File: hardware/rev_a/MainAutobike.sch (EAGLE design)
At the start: 137 parts, among them J13 TC2030-CTX, U1 ATUM, U2 PCA9685, U3 PCA9685, U4 ADXL362

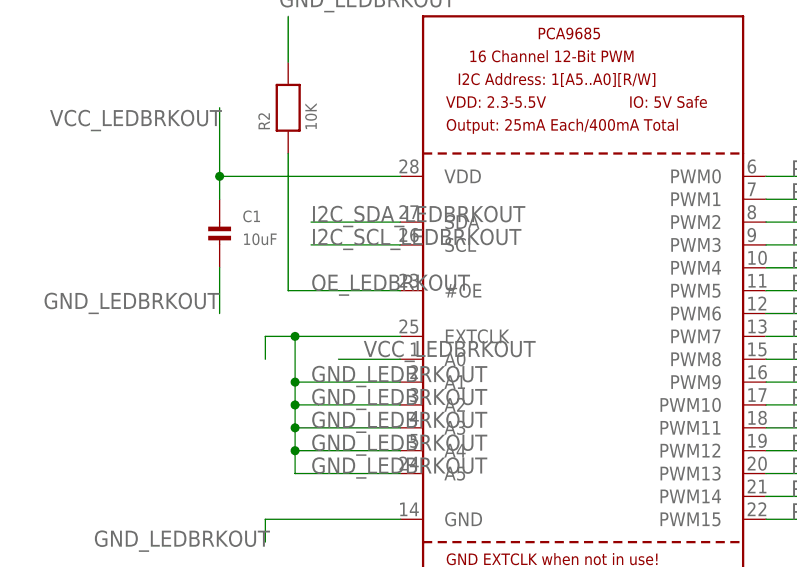
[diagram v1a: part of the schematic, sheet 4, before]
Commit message: charles, look over hall effect please; checked rest of schematic and board
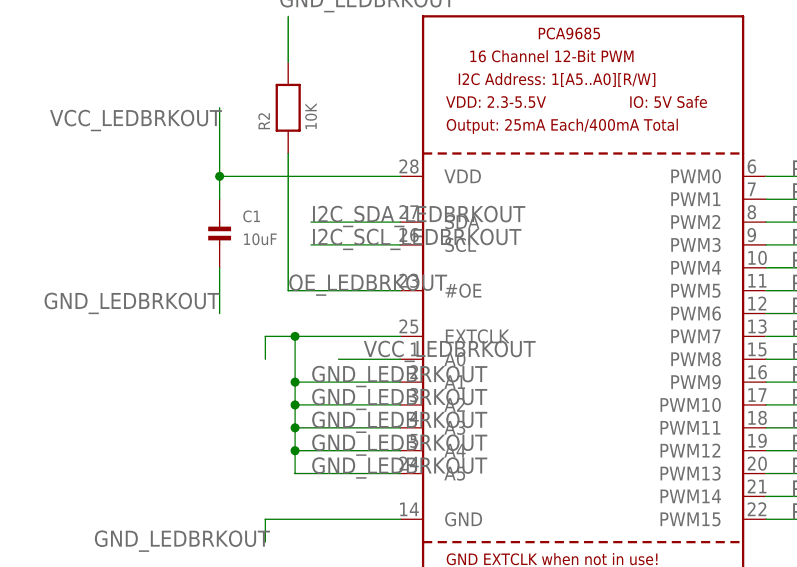
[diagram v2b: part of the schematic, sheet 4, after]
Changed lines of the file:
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@@
 <wire x1="-102.87" y1="-22.098" x2="-115.316" y2="-22.098" width="0.1524" layer="91"/>
 <wire x1="-115.316" y1="-22.098" x2="-115.316" y2="-6.858" width="0.1524" layer="91"/>
-<label x="-112.776" y="-22.098" size="1.778" layer="95"/>
+<label x="-115.316" y="-22.098" size="1.778" layer="95"/>
 <pinref part="U2" gate="G$1" pin="#OE"/>
 <pinref part="R2" gate="G$1" pin="1"/>

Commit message: final revision A of PCB
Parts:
- added DEC_GEAR_SWITCH1, INC_GEAR_SWITCH1: LED_SWITCH, led_switch:LED_SWITCH
- added GLED4: (no value), led:LEDCHIP-LED0603
- added JP13, JP14, JP15, JP19, JP8: (no value), pinhead:PINHD-1X4
- added JP16, JP17, JP18, JP20, JP9: (no value), pinhead:PINHD-1X3
- added JP21, JP22: (no value), pinhead:PINHD-1X2
- added R36, R45, R46, R47, R48: 10k, rcl:R-EU_R0603
- added R37, R39, R41, R42, R49: 1k, rcl:R-EU_R0603
- added R38, R40, R43, R44, R50: 390, rcl:R-EU_R0603
- added R51, R52, R53, R54, R55, R56, R57, R58: 33, rcl:R-US_R0402
- added R59: 60.4, rcl:R-US_R0402
- added U$20, U$22, U$23, U$24, U$25, U$28, U$29, U$31, U$32, U$34: 25AA02E48-SOT-23-6, 25AA02E48:25AA02E48-SOT-23-6
- added U$21, U$26, U$27, U$30, U$33: HALLEFFECT, 25AA02E48:HALLEFFECT
- JP1, JP2, JP3: device pinhead:PINHD-1X3 -> pinhead:PINHD-1X4
- R1: device microbuilder:RESISTOR0805 -> rcl:R-EU_R0603
- R17, R18, R25: value 1k -> 10k
- R2: device microbuilder:RESISTOR0805 -> rcl:R-US_R0603
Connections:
- net N$20 renamed VCC_LGT1
- net N$27 renamed VCC_LGT2
- net N$31 renamed VCC_LGT3
- new net GND_LGT1: JP1.4, R17.1
- new net GND_LGT2: JP2.4, R25.1
- new net GND_LGT3: JP3.4, R18.1
- new net GND_LGT4: JP8.4, R36.1
- new net GND_LGT5: JP13.4, R45.1
- new net GND_LGT6: JP14.4, R47.1
- new net GND_LGT7: JP15.4, R46.1
- new net GND_LGT8: JP19.4, R48.1
- new net HE4GND: JP9.3, U$21.GND, U$22.SRC
- new net HE4OUT: JP9.2, R38.1, U$22.DRN
- new net HE4VIN: JP9.1, R38.2, U$21.VCC
- new net HE5GND: JP16.3, U$30.GND, U$31.SRC
- new net HE5OUT: JP16.2, R40.1, U$31.DRN
- new net HE5VIN: JP16.1, R40.2, U$30.VCC
- new net HE6GND: JP17.3, U$26.GND, U$28.SRC
- new net HE6OUT: JP17.2, R43.1, U$28.DRN
- new net HE6VIN: JP17.1, R43.2, U$26.VCC
- new net HE7GND: JP18.3, U$27.GND, U$29.SRC
- new net HE7OUT: JP18.2, R44.1, U$29.DRN
- new net HE7VIN: JP18.1, R44.2, U$27.VCC
- new net HE8GND: JP20.3, U$33.GND, U$34.SRC
- new net HE8OUT: JP20.2, R50.1, U$34.DRN
- new net HE8VIN: JP20.1, R50.2, U$33.VCC
- new net N$19: R39.2, U$30.VOUT
- new net N$20: R41.1, U$29.GTE
- new net N$22: R41.2, U$27.VOUT
- new net N$27: R49.1, U$34.GTE
- new net N$31: JP14.3, R53.1
- new net N$33: JP8.3, R55.1
- new net N$34: JP3.3, R56.1
- new net N$39: JP2.3, R57.1
- new net N$42: JP1.3, R58.1
- new net N$43: INC_GEAR_SWITCH1.PIN1, JP21.2
- new net N$44: INC_GEAR_SWITCH1.PIN3, JP21.1
- new net N$45: DEC_GEAR_SWITCH1.PIN1, JP22.2
- new net N$49: DEC_GEAR_SWITCH1.PIN3, JP22.1
- new net N$79: GLED4.A, R59.1
- new net OUT_LGT1: R17.2, R58.2, U$15.SRC
- new net OUT_LGT2: R25.2, R57.2, U$16.SRC
- new net OUT_LGT3: R18.2, R56.2, U$17.SRC
- new net OUT_LGT4: R36.2, R55.2, U$20.SRC
- new net OUT_LGT5: R45.2, R54.2, U$23.SRC
- new net OUT_LGT6: R47.2, R53.2, U$24.SRC
- new net OUT_LGT7: R46.2, R52.2, U$25.SRC
- new net OUT_LGT8: R48.2, R51.2, U$32.SRC
- new net SIG_LGT1: JP1.2, U$15.GTE
- new net SIG_LGT2: JP2.2, U$16.GTE
- new net SIG_LGT3: JP3.2, U$17.GTE
- new net SIG_LGT4: JP8.2, U$20.GTE
- new net SIG_LGT5: JP13.2, U$23.GTE
- new net SIG_LGT6: JP14.2, U$24.GTE
- new net SIG_LGT7: JP15.2, U$25.GTE
- new net SIG_LGT8: JP19.2, U$32.GTE
- new net VCC_LGT4: JP8.1, U$20.DRN
- new net VCC_LGT5: JP13.1, U$23.DRN
- new net VCC_LGT6: JP14.1, U$24.DRN
- new net VCC_LGT7: JP15.1, U$25.DRN
- new net VCC_LGT8: JP19.1, U$32.DRN
- net N$13: now also R37.1, U$22.GTE; no longer JP1.2, R17.1
- net N$14: now also R37.2, U$21.VOUT; no longer R17.2, U$15.GTE
- net N$17: now also R39.1, U$31.GTE; no longer JP1.3, U$15.SRC
- net N$23: now also R42.1, U$28.GTE; no longer JP2.2, R25.1
- net N$26: now also R42.2, U$26.VOUT; no longer R25.2, U$16.GTE
- net N$28: now also R49.2, U$33.VOUT; no longer JP2.3, U$16.SRC
- net N$29: now also JP19.3, R51.1; no longer JP3.2, R18.1
- net N$30: now also JP15.3, R52.1; no longer R18.2, U$17.GTE
- net N$32: now also JP13.3, R54.1; no longer JP3.3, U$17.SRC
- net VCC(3.3V): now also R59.2

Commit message: crap...
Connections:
- net GND: now also GLED4.C
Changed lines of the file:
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@@
 <?xml version="1.0" encoding="utf-8"?>
 <!DOCTYPE eagle SYSTEM "eagle.dtd">
-<eagle version="6.6.0">
+<eagle version="6.4">
 <drawing>
 <settings>
@@
 <wire x1="284.734" y1="130.302" x2="284.734" y2="125.222" width="0.1524" layer="91"/>
 </segment>
+<segment>
+<pinref part="GLED4" gate="G$1" pin="C"/>
+<wire x1="171.704" y1="68.834" x2="171.704" y2="73.914" width="0.1524" layer="91"/>
+</segment>
 </net>
